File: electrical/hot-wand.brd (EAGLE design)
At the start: 112 x 72 mm, 181 parts, among them IC1 12V R-78K12-2.0, IC2 3V3 R-78K3.3, Q1 STP19NF20, Q2 IRF510, Q3 BC846B, Q4 SIRS5800DP-T1-GE3, Q5 SSM3K388R,LF, Q6 DMTH64M2LPDWQ-13, Q7 G3404, U1 TPS54560DDA, U2 1EDN8511BXUSA1, U3 INA138, U4 LM74700QDBVTQ1, U5 AP53781, U6 SSD1306-4PIN-0.91N-VERT, U7 STM32F030F4P6, Y1 27.12 MHz 10pF

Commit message: DFM changes, almost ready to order from JLC
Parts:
- C7: value 100nF -> 100n
- Q5: value SSM3K388R,LF -> 2N7002K
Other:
- board text added: "DNP"

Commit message: schematic preview generator
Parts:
- removed D13: (no value), hot-wand:SMA-DIODE
- removed D17: 3V6, hot-wand:SOD-323
- added TVS1: SM15T150CA, hot-wand:SMC
- added TVS2: SMBJ15CA, hot-wand:SMA-DIODE
- D10: value SMBJ15CA -> 2A
- D11: value STPS0540Z -> (none); device hot-wand:SOD123FL -> hot-wand:SMA-DIODE
- D12: value 2A -> 3V6; device hot-wand:SMA-DIODE -> hot-wand:SOD-323
- D9: value SM15T150CA -> STPS0540Z; device hot-wand:SMC -> hot-wand:SOD123FL
- FAN2: value FAN-TIEDOWN-20MM-V1 -> (none)
- moved D11 60.7 mm to (32.5, 29.0), turned to 0 degrees
- moved D12 41.6 mm to (35.9, 2.60)
- moved D10 36.0 mm to (40.0, 44.0), turned to 180 degrees
- moved D9 14.5 mm to (80.0, 66.8)
- renumbered D14 to TVS3, D15 to TVS4, D16 to TVS5
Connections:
- net +12V: now also D10.C; no longer D12.C
- net 12V-2: now also D10.A; no longer D12.A
- net 3.3V: now also D11.A; no longer D13.A
- net BTN: now also D12.1; no longer D17.1
- net DC-IN: now also D11.C; no longer D13.C
- net GND: now also D12.2, TVS1.A, TVS2.A; no longer D10.A, D11.A, D17.2
- net N$7: now also TVS1.C; no longer D9.C
- net RF-GATE: now also D9.C, TVS2.C; no longer D10.C, D11.C

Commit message: enclosure work
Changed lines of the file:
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@@
 <grid distance="0.1" unitdist="mm" unit="mm" style="lines" multiple="10" display="yes" altdistance="0.02" altunitdist="mm" altunit="mm"/>
 <layers>
-<layer number="1" name="Top" color="4" fill="1" visible="no" active="yes"/>
+<layer number="1" name="Top" color="4" fill="1" visible="yes" active="yes"/>
 <layer number="2" name="Route2" color="1" fill="3" visible="no" active="no"/>
 <layer number="3" name="Route3" color="4" fill="3" visible="no" active="no"/>
@@
 <layer number="19" name="Unrouted" color="6" fill="1" visible="yes" active="yes"/>
 <layer number="20" name="Dimension" color="15" fill="1" visible="yes" active="yes"/>
-<layer number="21" name="tPlace" color="7" fill="1" visible="no" active="yes"/>
+<layer number="21" name="tPlace" color="7" fill="1" visible="yes" active="yes"/>
 <layer number="22" name="bPlace" color="7" fill="1" visible="yes" active="yes"/>
 <layer number="23" name="tOrigins" color="15" fill="1" visible="yes" active="yes"/>
 <layer number="24" name="bOrigins" color="15" fill="1" visible="yes" active="yes"/>
-<layer number="25" name="tNames" color="7" fill="1" visible="no" active="yes"/>
+<layer number="25" name="tNames" color="7" fill="1" visible="yes" active="yes"/>
 <layer number="26" name="bNames" color="7" fill="1" visible="yes" active="yes"/>
-<layer number="27" name="tValues" color="7" fill="1" visible="no" active="yes"/>
+<layer number="27" name="tValues" color="7" fill="1" visible="yes" active="yes"/>
 <layer number="28" name="bValues" color="7" fill="1" visible="yes" active="yes"/>
 <layer number="29" name="tStop" color="7" fill="3" visible="no" active="yes"/>
-<layer number="30" name="bStop" color="7" fill="6" visible="yes" active="yes"/>
+<layer number="30" name="bStop" color="7" fill="6" visible="no" active="yes"/>
 <layer number="31" name="tCream" color="7" fill="4" visible="no" active="yes"/>
-<layer number="32" name="bCream" color="7" fill="5" visible="yes" active="yes"/>
+<layer number="32" name="bCream" color="7" fill="5" visible="no" active="yes"/>
 <layer number="33" name="tFinish" color="6" fill="3" visible="no" active="yes"/>
 <layer number="34" name="bFinish" color="6" fill="6" visible="no" active="yes"/>
@@
 </element>
 <element name="SW1" library="hot-wand" package="SW_1-1825027-1" value="" x="37" y="4.5" smashed="yes">
-<attribute name="PARTNUM" value="TL1105RF250Q" x="37" y="4.5" size="1.778" layer="27" display="off"/>
+<attribute name="PARTNUM" value="MJTP1236D;TL1105JAF160R1RBLK" x="37" y="4.5" size="1.778" layer="27" display="off"/>
 <attribute name="COMMENT" value="1-1825027-1" x="37" y="4.5" size="1.778" layer="27" display="off"/>
 <attribute name="MF" value="TE Connectivity" x="37" y="4.5" size="1.778" layer="27" display="off"/>
@@
 <via x="48.4" y="11.2" extent="1-16" drill="0.3" shape="octagon"/>
 <via x="49.8" y="11.2" extent="1-16" drill="0.3" shape="octagon"/>
-<via x="49.1" y="9.7" extent="1-16" drill="0.3" shape="octagon"/>
+<via x="49.8" y="9.5" extent="1-16" drill="0.3" shape="octagon"/>
 <via x="45.7" y="20.6" extent="1-16" drill="0.3" shape="octagon"/>
 <via x="42.4" y="11" extent="1-16" drill="0.3" shape="octagon"/>
@@
 <wire x1="40.375" y1="15.12" x2="40.375" y2="10.425" width="0.2032" layer="16"/>
 <wire x1="40.375" y1="10.425" x2="42.8" y2="8" width="0.2032" layer="16"/>
-<wire x1="42.8" y1="8" x2="45.8" y2="8" width="0.2032" layer="16"/>
-<wire x1="45.8" y1="8" x2="47.19" y2="6.61" width="0.2032" layer="16"/>
-<wire x1="47.19" y1="6.61" x2="47.19" y2="5" width="0.2032" layer="16"/>
+<wire x1="42.8" y1="8" x2="45.8" y2="8" width="0.254" layer="16"/>
+<wire x1="45.8" y1="8" x2="47.19" y2="6.61" width="0.3048" layer="16"/>
+<wire x1="47.19" y1="6.61" x2="47.19" y2="5" width="0.4064" layer="16"/>
 <contactref element="R35" pad="1"/>
-<wire x1="47.19" y1="5" x2="47.19" y2="2.9" width="0.2032" layer="16"/>
+<wire x1="47.19" y1="5" x2="47.19" y2="2.9" width="0.4064" layer="16"/>
 <wire x1="47.19" y1="2.9" x2="46.95" y2="2.9" width="0.2032" layer="16"/>
 </signal>
@@
 <wire x1="41.025" y1="15.12" x2="41.025" y2="11.475" width="0.2032" layer="16"/>
 <wire x1="41.025" y1="11.475" x2="43.6" y2="9.1" width="0.2032" layer="16"/>
-<wire x1="43.6" y1="9.1" x2="47.4" y2="9.1" width="0.2032" layer="16"/>
-<wire x1="47.4" y1="9.1" x2="49.73" y2="6.77" width="0.2032" layer="16"/>
-<wire x1="49.73" y1="6.77" x2="49.73" y2="5" width="0.2032" layer="16"/>
+<wire x1="43.6" y1="9.1" x2="47.4" y2="9.1" width="0.254" layer="16"/>
+<wire x1="47.4" y1="9.1" x2="49.73" y2="6.77" width="0.3048" layer="16"/>
+<wire x1="49.73" y1="6.77" x2="49.73" y2="5" width="0.4064" layer="16"/>
 <contactref element="R36" pad="1"/>
-<wire x1="49.73" y1="5" x2="49.73" y2="2.9" width="0.2032" layer="16"/>
-<wire x1="49.73" y1="2.9" x2="50.15" y2="2.9" width="0.2032" layer="16"/>
+<wire x1="49.73" y1="5" x2="49.73" y2="3.3" width="0.4064" layer="16"/>
+<wire x1="49.73" y1="3.3" x2="50.15" y2="2.9" width="0.2032" layer="16"/>
 </signal>
 <signal name="N$33">

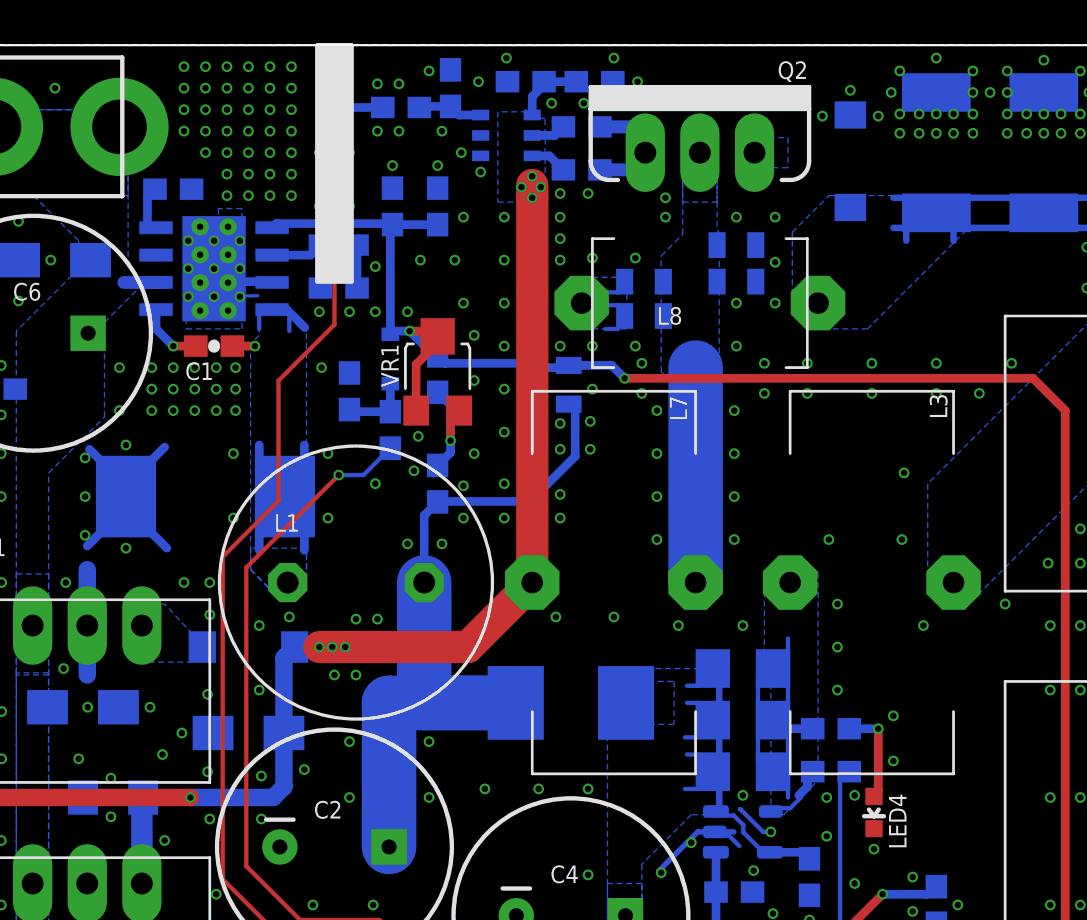
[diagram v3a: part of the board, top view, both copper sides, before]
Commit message: added a current sensor for 12V current draw
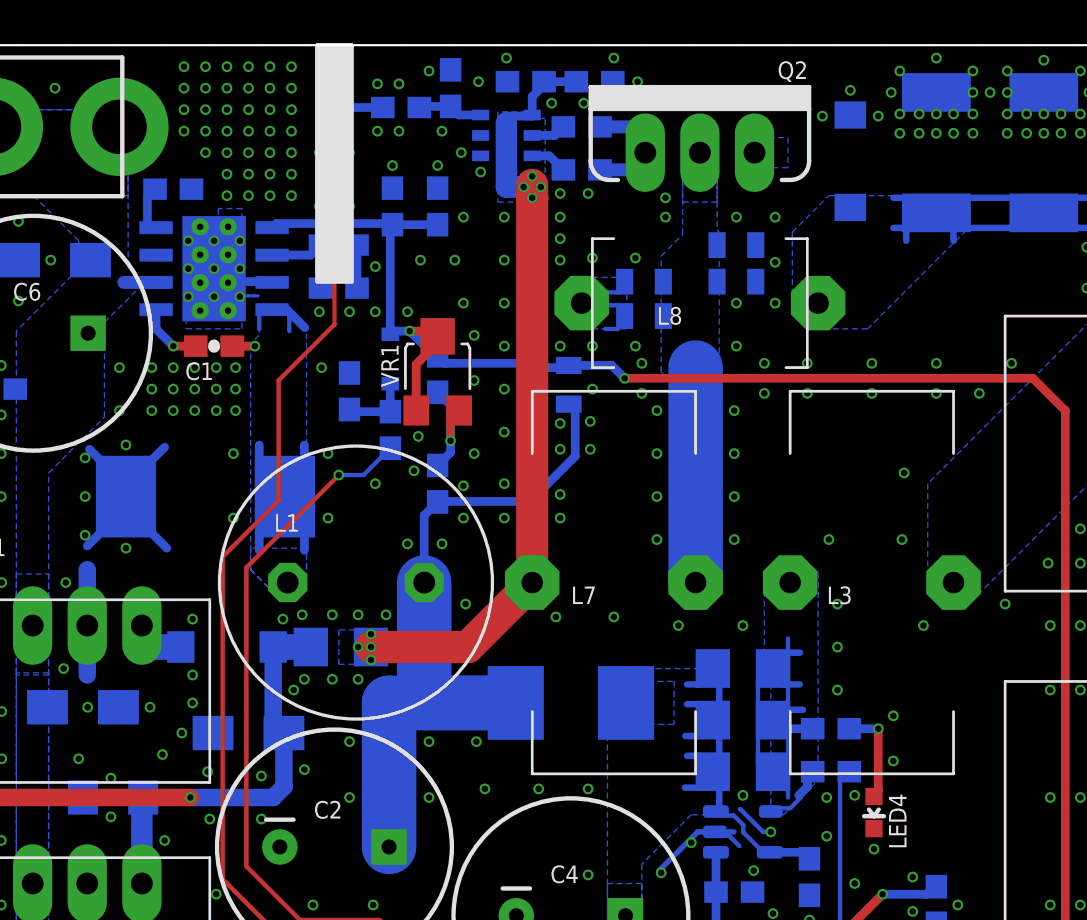
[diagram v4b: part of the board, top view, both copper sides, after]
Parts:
- added R48: (no value), hot-wand:1206
- moved D10 1.00 mm to (39.0, 44.0)
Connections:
- new net N$58: C35.2, C36.2, L7.2, R48.2, U2.1
- net +12V: now also R48.1; no longer C35.2, C36.2, L7.2, U2.1
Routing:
- net N$58: track 0.00 -> 36.3 mm, vias 0 -> 8
- net +12V: track 71.7 -> 38.5 mm, vias 9 -> 2
- net 12V-2: track 0.00 -> 2.81 mm
- net +24V: track 16.0 -> 18.5 mm
- net GND: vias 666 -> 669
- added copper zone on layer 16, net N$58
- removed copper zone on layer 16, net +12V
- removed copper zone on layer 16, net 12V-2

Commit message: major thermal related changes, and I moved that one bootstrap cap to the bottom
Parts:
- moved C1 4.02 mm to (34.4, 57.6), flipped to the bottom, turned to 270 degrees
- moved LED1 1.00 mm to (27.1, 51.7)
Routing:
- net N$23: track 15.1 -> 21.9 mm, vias 1 -> 2
- net N$22: track 3.08 -> 1.96 mm, vias 1 -> 0
- net N$46: track 2.90 -> 3.90 mm
- net GND: vias 669 -> 674

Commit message: circuit drill sizes sorted
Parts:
- SW1: value (none) -> SW-TACT-SIDE
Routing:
- net GND: vias 674 -> 679
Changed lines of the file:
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@@
 <layer number="23" name="tOrigins" color="15" fill="1" visible="yes" active="yes"/>
 <layer number="24" name="bOrigins" color="15" fill="1" visible="yes" active="yes"/>
-<layer number="25" name="tNames" color="7" fill="1" visible="yes" active="yes"/>
+<layer number="25" name="tNames" color="7" fill="1" visible="no" active="yes"/>
 <layer number="26" name="bNames" color="7" fill="1" visible="yes" active="yes"/>
-<layer number="27" name="tValues" color="7" fill="1" visible="yes" active="yes"/>
+<layer number="27" name="tValues" color="7" fill="1" visible="no" active="yes"/>
 <layer number="28" name="bValues" color="7" fill="1" visible="yes" active="yes"/>
 <layer number="29" name="tStop" color="7" fill="3" visible="no" active="yes"/>
@@
 </polygon>
 <text x="43" y="41.9" size="0.8128" layer="28" rot="MR180">DNP</text>
+<wire x1="13.4" y1="42.4" x2="13.4" y2="37.6" width="0.4064" layer="21"/>
+<wire x1="17.9" y1="52.3" x2="17.9" y2="47.5" width="0.4064" layer="21"/>
 </plain>
 <attributes>
@@
 <attribute name="JLC-DNP" value="1" x="68.5" y="7" size="1.778" layer="27" rot="R180" display="off"/>
 </element>
-<element name="SW1" library="hot-wand" package="SW_1-1825027-1" value="" x="37" y="4.5" smashed="yes">
+<element name="SW1" library="hot-wand" package="SW_1-1825027-1" value="SW-TACT-SIDE" x="37" y="4.5" smashed="yes">
 <attribute name="PARTNUM" value="MJTP1236D;TL1105JAF160R1RBLK" x="37" y="4.5" size="1.778" layer="27" display="off"/>
 <attribute name="COMMENT" value="1-1825027-1" x="37" y="4.5" size="1.778" layer="27" display="off"/>
@@
 <via x="20.12" y="39.6" extent="1-16" drill="0.3" shape="octagon"/>
 <via x="20.02" y="37.6" extent="1-16" drill="0.3" shape="octagon"/>
-<via x="16.42" y="36.5" extent="1-16" drill="0.3" shape="octagon"/>
-<via x="16.42" y="35" extent="1-16" drill="0.3" shape="octagon"/>
+<via x="16.52" y="36.5" extent="1-16" drill="0.3" shape="octagon"/>
+<via x="16.52" y="35" extent="1-16" drill="0.3" shape="octagon"/>
 <via x="18.02" y="35" extent="1-16" drill="0.3" shape="octagon"/>
 <via x="20.02" y="35" extent="1-16" drill="0.3" shape="octagon"/>
@@
 <via x="44.9" y="13" extent="1-16" drill="0.3" shape="octagon"/>
 <via x="43.1" y="19.5" extent="1-16" drill="0.3" shape="octagon"/>
-<via x="36.3" y="19.9" extent="1-16" drill="0.3" shape="octagon"/>
+<via x="36.2" y="19.9" extent="1-16" drill="0.3" shape="octagon"/>
 <via x="36.4" y="18.7" extent="1-16" drill="0.3" shape="octagon"/>
 <via x="41" y="18.7" extent="1-16" drill="0.3" shape="octagon"/>
@@
 <via x="32.2" y="11.9" extent="1-16" drill="0.3" shape="octagon"/>
 <via x="30.2" y="8.1" extent="1-16" drill="0.3" shape="octagon"/>
-<via x="29.2" y="8.9" extent="1-16" drill="0.3" shape="octagon"/>
+<via x="29" y="8.8" extent="1-16" drill="0.3" shape="octagon"/>
 <via x="27" y="4.9" extent="1-16" drill="0.3" shape="octagon"/>
 <via x="28.9" y="4.9" extent="1-16" drill="0.3" shape="octagon"/>
@@
 <via x="19.7" y="4" extent="1-16" drill="0.3" shape="octagon"/>
 <via x="24.8" y="4.4" extent="1-16" drill="0.3" shape="octagon"/>
-<via x="26.8" y="3.3" extent="1-16" drill="0.3" shape="octagon"/>
+<via x="26.7" y="3.5" extent="1-16" drill="0.3" shape="octagon"/>
 <via x="30" y="3" extent="1-16" drill="0.3" shape="octagon"/>
 <via x="30" y="1" extent="1-16" drill="0.3" shape="octagon"/>
@@
 <via x="33.2" y="55.1" extent="1-16" drill="0.3" shape="octagon"/>
 <via x="32.4" y="54.3" extent="1-16" drill="0.3" shape="octagon"/>
+<via x="77" y="62.6" extent="1-16" drill="0.3" shape="octagon"/>
+<via x="75" y="62.6" extent="1-16" drill="0.3" shape="octagon"/>
+<via x="73" y="61.5" extent="1-16" drill="0.3" shape="octagon"/>
+<via x="71" y="59.5" extent="1-16" drill="0.3" shape="octagon"/>
+<via x="29" y="6.8" extent="1-16" drill="0.3" shape="octagon"/>
 </signal>
 <signal name="RF-OUT">
@@
 <wire x1="13.4" y1="36.8" x2="12.9" y2="37.3" width="0.2032" layer="1"/>
 <wire x1="12.9" y1="37.3" x2="12.9" y2="38.095" width="0.2032" layer="1"/>
-<wire x1="13.4" y1="35.75" x2="13.4" y2="36.8" width="0.2032" layer="16"/>
+<wire x1="13.4" y1="35.75" x2="13.4" y2="36.8" width="0.4064" layer="16"/>
 </signal>
 <signal name="N$39">
@@
 <via x="11" y="38.5" extent="1-16" drill="0.3" shape="octagon"/>
 <contactref element="TVS5" pad="C"/>
-<wire x1="15.35" y1="31" x2="15.8" y2="31" width="0.2032" layer="16"/>
-<wire x1="15.8" y1="31" x2="15.8" y2="35.5" width="0.2032" layer="16"/>
-<wire x1="15.8" y1="35.8" x2="15.8" y2="39.491725" width="0.2032" layer="16"/>
-<wire x1="15.8" y1="39.491725" x2="15.191725" y2="40.1" width="0.2032" layer="16"/>
-<wire x1="15.191725" y1="40.1" x2="11" y2="40.1" width="0.2032" layer="16"/>
-<wire x1="11" y1="40.1" x2="11" y2="38.5" width="0.2032" layer="16"/>
+<wire x1="15.35" y1="31" x2="15.8" y2="31" width="0.3048" layer="16"/>
+<wire x1="15.8" y1="31" x2="15.8" y2="35.8" width="0.3048" layer="16"/>
+<wire x1="15.8" y1="35.8" x2="15.8" y2="39.391725" width="0.3048" layer="16"/>
+<wire x1="15.8" y1="39.391725" x2="15.191725" y2="40" width="0.3048" layer="16"/>
+<wire x1="15.191725" y1="40" x2="11" y2="40" width="0.3048" layer="16"/>
+<wire x1="11" y1="40" x2="11" y2="38.5" width="0.2032" layer="16"/>
 <wire x1="11" y1="38.5" x2="10.3" y2="38.5" width="0.2032" layer="16"/>
 <wire x1="10.3" y1="38.5" x2="10.3" y2="39.2" width="0.2032" layer="16"/>
-<wire x1="21.15" y1="35.8" x2="15.8" y2="35.8" width="0.2032" layer="16"/>
-<wire x1="15.8" y1="35.8" x2="15.8" y2="35.5" width="0.2032" layer="16"/>
+<wire x1="21.15" y1="35.8" x2="15.8" y2="35.8" width="0.3048" layer="16"/>
 </signal>
 <signal name="N$35">
@@
 <wire x1="30.3" y1="19.3" x2="17.84" y2="6.84" width="0.2032" layer="16"/>
 <wire x1="17.84" y1="6.84" x2="17.84" y2="6.2" width="0.2032" layer="16"/>
-<wire x1="17.84" y1="6.2" x2="17.84" y2="2" width="0.2032" layer="16"/>
+<wire x1="17.84" y1="6.2" x2="17.84" y2="1.9" width="0.2032" layer="16"/>
 <wire x1="18.25" y1="6.2" x2="17.84" y2="6.2" width="0.2032" layer="16"/>
 </signal>
@@
 <wire x1="39.075" y1="14.5" x2="35.7" y2="14.5" width="0.2032" layer="16"/>
 <wire x1="35.7" y1="14.5" x2="25.46" y2="4.26" width="0.2032" layer="16"/>
-<wire x1="25.46" y1="4.26" x2="25.46" y2="2.254" width="0.2032" layer="16"/>
+<wire x1="25.46" y1="4.26" x2="25.46" y2="2.354" width="0.2032" layer="16"/>
 </signal>
 <signal name="SWDIO">
@@
 <wire x1="39.5114" y1="16.4" x2="32.4" y2="16.4" width="0.2032" layer="16"/>
 <wire x1="32.4" y1="16.4" x2="20.38" y2="4.38" width="0.2032" layer="16"/>
-<wire x1="20.38" y1="4.38" x2="20.38" y2="2.254" width="0.2032" layer="16"/>
+<wire x1="20.38" y1="4.38" x2="20.38" y2="2.354" width="0.2032" layer="16"/>
 <contactref element="SJ5" pad="2"/>
 <via x="30.6" y="20.6" extent="1-16" drill="0.3" shape="octagon"/>
